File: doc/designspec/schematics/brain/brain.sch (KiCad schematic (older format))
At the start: 6 parts

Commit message: Add component lib
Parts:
- removed P?: Raspberry Pi 3 GPIO, symbol Raspberry~Pi~3~GPIO
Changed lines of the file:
@@
 $EndDescr
-$Comp
-L Raspberry~Pi~3~GPIO P?
-U 1 1 57FD3D22
-P 2800 2000
-F 0 "P?" H 2800 3050 50  0000 C CNN
-F 1 "Raspberry Pi 3 GPIO" V 2800 2000 50  0000 C CNN
-F 2 "" H 2800 1050 50  0000 C CNN
-F 3 "" H 2800 1050 50  0000 C CNN
-	1    2800 2000
-	1    0    0    -1
-$EndComp
 $Comp
 L USB_A P?
@@
 F 1 "CH340G" H 3800 4300 60  0000 C CNN
 F 2 "" H 3800 4300 60  0001 C CNN
-F 3 "" H 3800 4300 60  0001 C CNN
+F 3 "TODO: Choose component" H 3800 4300 60  0001 C CNN
 	1    3800 4300
 	-1   0    0    1
@@
 F 1 "CH340G" H 3800 3450 60  0000 C CNN
 F 2 "" H 3800 3450 60  0001 C CNN
-F 3 "" H 3800 3450 60  0001 C CNN
+F 3 "TODO: Choose component" H 3800 3450 60  0001 C CNN
 	1    3800 3450
 	-1   0    0    1

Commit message: Fix error for rpi_gpio in lib
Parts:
- added P?: Raspberry_pi_3_gpio, symbol Raspberry_pi_3_gpio
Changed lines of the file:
@@
 	1    0    0    -1
 $EndComp
-NoConn ~ 2350 2950
-NoConn ~ 2350 2850
-NoConn ~ 2350 2750
-NoConn ~ 2350 2650
-NoConn ~ 2350 2550
-NoConn ~ 2350 2450
-NoConn ~ 2350 2350
-NoConn ~ 2350 2250
-NoConn ~ 2350 2150
-NoConn ~ 2350 2050
-NoConn ~ 2350 1950
-NoConn ~ 2350 1850
-NoConn ~ 2350 1750
-NoConn ~ 2350 1650
-NoConn ~ 2350 1550
-NoConn ~ 2350 1450
-NoConn ~ 2350 1350
-NoConn ~ 2350 1250
-NoConn ~ 2350 1150
-NoConn ~ 2350 1050
+NoConn ~ 2750 2950
+NoConn ~ 2750 2850
+NoConn ~ 2750 2750
+NoConn ~ 2750 2650
+NoConn ~ 2750 2550
+NoConn ~ 2750 2450
+NoConn ~ 2750 2350
+NoConn ~ 2750 2250
+NoConn ~ 2750 2150
+NoConn ~ 2750 2050
+NoConn ~ 2750 1950
+NoConn ~ 2750 1850
+NoConn ~ 2750 1750
+NoConn ~ 2750 1650
+NoConn ~ 2750 1550
+NoConn ~ 2750 1450
+NoConn ~ 2750 1350
+NoConn ~ 2750 1250
+NoConn ~ 2750 1150
+NoConn ~ 2750 1050
 NoConn ~ 3250 1050
 NoConn ~ 3250 1150
@@
 NoConn ~ 3250 2650
 NoConn ~ 3250 2750
+$Comp
+L Raspberry_pi_3_gpio P?
+U 1 1 57FD5699
+P 3000 2000
+F 0 "P?" H 3000 3050 50  0000 C CNN
+F 1 "Raspberry_pi_3_gpio" V 3000 2000 50  0000 C CNN
+F 2 "" H 3000 1050 50  0000 C CNN
+F 3 "" H 3000 1050 50  0000 C CNN
+	1    3000 2000
+	1    0    0    -1
+$EndComp
 $EndSCHEMATC

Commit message: Fix rpi pins
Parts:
- removed P?: Raspberry_pi_3_gpio, symbol Raspberry_pi_3_gpio
- added P3: Raspberry Pi 3 GPIO, symbol Raspberry~Pi~3~GPIO
- gave numbers to parts that had none: 5
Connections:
- net labels added: +3.3V
- net labels removed: +5V
- wire segments 8 -> 10
- no-connect marks 42 -> 41
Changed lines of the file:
@@
 $EndDescr
 $Comp
-L USB_A P?
+L USB_A P2
 U 1 1 57FD3DF3
 P 2950 4250
-F 0 "P?" H 3150 4050 50  0000 C CNN
+F 0 "P2" H 3150 4050 50  0000 C CNN
 F 1 "USB_RPi_1" H 2900 4450 50  0000 C CNN
 F 2 "" V 2900 4150 50  0000 C CNN
@@
 $EndComp
 $Comp
-L USB_A P?
+L USB_A P1
 U 1 1 57FD409A
 P 2950 3400
-F 0 "P?" H 3150 3200 50  0000 C CNN
+F 0 "P1" H 3150 3200 50  0000 C CNN
 F 1 "USB_RPi_2" H 2900 3600 50  0000 C CNN
 F 2 "" V 2900 3300 50  0000 C CNN
@@
 $EndComp
 $Comp
-L CH340G U?
+L CH340G U2
 U 1 1 57FD4430
 P 3800 4300
-F 0 "U?" H 3450 4650 60  0000 C CNN
+F 0 "U2" H 3450 4650 60  0000 C CNN
 F 1 "CH340G" H 3800 4300 60  0000 C CNN
 F 2 "" H 3800 4300 60  0001 C CNN
@@
 $EndComp
 $Comp
-L CH340G U?
+L CH340G U1
 U 1 1 57FD4518
 P 3800 3450
-F 0 "U?" H 3450 3800 60  0000 C CNN
+F 0 "U1" H 3450 3800 60  0000 C CNN
 F 1 "CH340G" H 3800 3450 60  0000 C CNN
 F 2 "" H 3800 3450 60  0001 C CNN
@@
 $EndComp
 $Comp
-L BTN U?
+L BTN U3
 U 1 1 57FD4666
 P 3900 2800
-F 0 "U?" H 4050 2550 60  0000 C CNN
+F 0 "U3" H 4050 2550 60  0000 C CNN
 F 1 "BTN x2" H 3800 2800 60  0000 C CNN
 F 2 "" H 3900 2800 60  0001 C CNN
@@
 NoConn ~ 3500 2950
 $Comp
-L +5V #PWR?
-U 1 1 57FD4995
-P 4400 2650
-F 0 "#PWR?" H 4400 2500 50  0001 C CNN
-F 1 "+5V" H 4400 2790 50  0000 C CNN
-F 2 "" H 4400 2650 50  0000 C CNN
-F 3 "" H 4400 2650 50  0000 C CNN
-	1    4400 2650
-	1    0    0    -1
-$EndComp
-$Comp
-L GND #PWR?
+L GND #PWR01
 U 1 1 57FD49B5
 P 4400 2950
-F 0 "#PWR?" H 4400 2700 50  0001 C CNN
+F 0 "#PWR01" H 4400 2700 50  0001 C CNN
 F 1 "GND" H 4400 2800 50  0000 C CNN
 F 2 "" H 4400 2950 50  0000 C CNN
@@
 NoConn ~ 2750 1250
 NoConn ~ 2750 1150
-NoConn ~ 2750 1050
 NoConn ~ 3250 1050
 NoConn ~ 3250 1150
@@
 NoConn ~ 3250 2650
 NoConn ~ 3250 2750
+Wire Wire Line
+	2750 1050 2600 1050
 $Comp
-L Raspberry_pi_3_gpio P?
-U 1 1 57FD5699
+L +3.3V #PWR02
+U 1 1 57FE3030
+P 2600 1050
+F 0 "#PWR02" H 2600 900 50  0001 C CNN
+F 1 "+3.3V" H 2600 1190 50  0000 C CNN
+F 2 "" H 2600 1050 50  0000 C CNN
+F 3 "" H 2600 1050 50  0000 C CNN
+	1    2600 1050
+	1    0    0    -1
+$EndComp
+$Comp
+L +3.3V #PWR03
+U 1 1 57FE3059
+P 4400 2650
+F 0 "#PWR03" H 4400 2500 50  0001 C CNN
+F 1 "+3.3V" H 4400 2790 50  0000 C CNN
+F 2 "" H 4400 2650 50  0000 C CNN
+F 3 "" H 4400 2650 50  0000 C CNN
+	1    4400 2650
+	1    0    0    -1
+$EndComp
+$Comp
+L Raspberry~Pi~3~GPIO P3
+U 1 1 57FE33DC
 P 3000 2000
-F 0 "P?" H 3000 3050 50  0000 C CNN
-F 1 "Raspberry_pi_3_gpio" V 3000 2000 50  0000 C CNN
+F 0 "P3" H 3000 3050 50  0000 C CNN
+F 1 "Raspberry Pi 3 GPIO" V 3000 2000 50  0000 C CNN
 F 2 "" H 3000 1050 50  0000 C CNN
 F 3 "" H 3000 1050 50  0000 C CNN
@@
 	1    0    0    -1
 $EndComp
+Wire Wire Line
+	3250 1250 3450 1250
+$Comp
+L GND #PWR04
+U 1 1 57FE3423
+P 3450 1250
+F 0 "#PWR04" H 3450 1000 50  0001 C CNN
+F 1 "GND" H 3450 1100 50  0000 C CNN
+F 2 "" H 3450 1250 50  0000 C CNN
+F 3 "" H 3450 1250 50  0000 C CNN
+	1    3450 1250
+	1    0    0    -1
+$EndComp

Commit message: Fix RPI in lib (dont use spaces in component names)
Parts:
- removed P3: Raspberry Pi 3 GPIO, symbol Raspberry~Pi~3~GPIO
- added P3: RPi_3_GPIO, symbol RPi_3_GPIO
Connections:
- no-connect marks 41 -> 40
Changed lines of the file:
@@
 NoConn ~ 3250 1050
 NoConn ~ 3250 1150
-NoConn ~ 3250 1250
 NoConn ~ 3250 1350
 NoConn ~ 3250 1450
@@
 	1    0    0    -1
 $EndComp
-$Comp
-L Raspberry~Pi~3~GPIO P3
-U 1 1 57FE33DC
-P 3000 2000
-F 0 "P3" H 3000 3050 50  0000 C CNN
-F 1 "Raspberry Pi 3 GPIO" V 3000 2000 50  0000 C CNN
-F 2 "" H 3000 1050 50  0000 C CNN
-F 3 "" H 3000 1050 50  0000 C CNN
-	1    3000 2000
-	1    0    0    -1
-$EndComp
 Wire Wire Line
 	3250 1250 3450 1250
@@
 	1    0    0    -1
 $EndComp
+$Comp
+L RPi_3_GPIO P3
+U 1 1 57FE32EC
+P 3000 2000
+F 0 "P3" H 3000 3050 50  0000 C CNN
+F 1 "RPi_3_GPIO" V 3000 2000 50  0000 C CNN
+F 2 "" H 3000 1050 50  0000 C CNN
+F 3 "" H 3000 1050 50  0000 C CNN
+	1    3000 2000
+	1    0    0    -1
+$EndComp

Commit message: Use simple switch instead of button
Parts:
- removed U3: BTN x2, symbol BTN
- added SW? (x2): SPST, symbol SPST
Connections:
- no-connect marks 40 -> 38
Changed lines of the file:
@@
-	-1   0    0    1
-$EndComp
-$Comp
-L BTN U3
-U 1 1 57FD4666
-P 3900 2800
-F 0 "U3" H 4050 2550 60  0000 C CNN
-F 1 "BTN x2" H 3800 2800 60  0000 C CNN
-F 2 "" H 3900 2800 60  0001 C CNN
-F 3 "" H 3900 2800 60  0001 C CNN
-	1    3900 2800
 	-1   0    0    1
 $EndComp
 NoConn ~ 4400 4350
 NoConn ~ 4400 3500
-Wire Wire Line
-	4400 4550 4400 4450
-Wire Wire Line
-	4400 3700 4400 3600
-Wire Wire Line
-	3350 2650 3500 2650
-Wire Wire Line
-	3350 2650 3350 2850
-Wire Wire Line
-	3350 2850 3250 2850
-Wire Wire Line
-	3500 2850 3450 2850
-Wire Wire Line
-	3450 2850 3450 2950
-Wire Wire Line
-	3450 2950 3250 2950
-NoConn ~ 3500 2750
-NoConn ~ 3500 2950
-$Comp
-L GND #PWR01
-U 1 1 57FD49B5
-P 4400 2950
-F 0 "#PWR01" H 4400 2700 50  0001 C CNN
-F 1 "GND" H 4400 2800 50  0000 C CNN
-F 2 "" H 4400 2950 50  0000 C CNN
-F 3 "" H 4400 2950 50  0000 C CNN
-	1    4400 2950
-	1    0    0    -1
-$EndComp
 NoConn ~ 2750 2950
 NoConn ~ 2750 2850
@@
 NoConn ~ 3250 2650
 NoConn ~ 3250 2750
-Wire Wire Line
-	2750 1050 2600 1050
 $Comp
 L +3.3V #PWR02
@@
 L +3.3V #PWR03
 U 1 1 57FE3059
-P 4400 2650
-F 0 "#PWR03" H 4400 2500 50  0001 C CNN
-F 1 "+3.3V" H 4400 2790 50  0000 C CNN
-F 2 "" H 4400 2650 50  0000 C CNN
-F 3 "" H 4400 2650 50  0000 C CNN
-	1    4400 2650
+P 4550 2850
+F 0 "#PWR03" H 4550 2700 50  0001 C CNN
+F 1 "+3.3V" H 4550 2990 50  0000 C CNN
+F 2 "" H 4550 2850 50  0000 C CNN
+F 3 "" H 4550 2850 50  0000 C CNN
+	1    4550 2850
 	1    0    0    -1
 $EndComp
-Wire Wire Line
-	3250 1250 3450 1250
 $Comp
 L GND #PWR04
@@
 	1    0    0    -1
 $EndComp
+$Comp
+L SPST SW?
+U 1 1 580118F0
+P 3850 2700
+F 0 "SW?" H 3850 2800 50  0000 C CNN
+F 1 "SPST" H 3850 2600 50  0000 C CNN
+F 2 "" H 3850 2700 50  0000 C CNN
+F 3 "" H 3850 2700 50  0000 C CNN
+	1    3850 2700
+	1    0    0    -1
+$EndComp
+Wire Wire Line
+	4400 4550 4400 4450
+Wire Wire Line
+	4400 3700 4400 3600
+Wire Wire Line
+	3350 2850 3250 2850
+Wire Wire Line
+	2750 1050 2600 1050
+Wire Wire Line
+	3250 1250 3450 1250
+Wire Wire Line
+	3350 2700 3350 2850
+$Comp
+L SPST SW?
+U 1 1 58011A78
+P 3850 3000
+F 0 "SW?" H 3850 3100 50  0000 C CNN
+F 1 "SPST" H 3850 2900 50  0000 C CNN
+F 2 "" H 3850 3000 50  0000 C CNN
+F 3 "" H 3850 3000 50  0000 C CNN
+	1    3850 3000
+	1    0    0    -1
+$EndComp
+Wire Wire Line
+	4350 2700 4350 3000
+Wire Wire Line
+	3250 2950 3350 2950
+Wire Wire Line
+	3350 2950 3350 3000
+Wire Wire Line
+	4350 2850 4550 2850
+Connection ~ 4350 2850
 $EndSCHEMATC

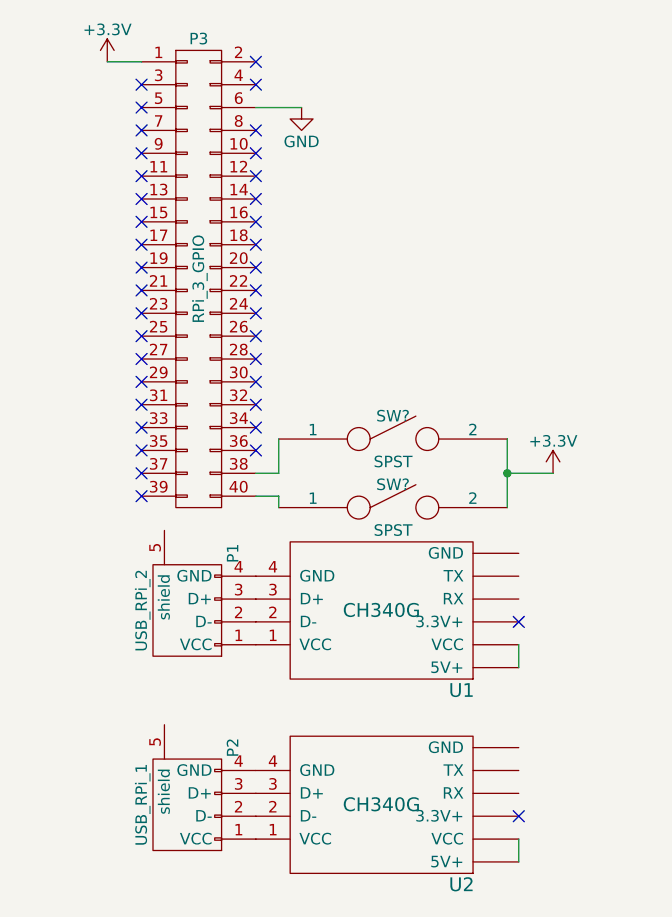
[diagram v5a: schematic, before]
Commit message: Replace CH340G with general USB-UART
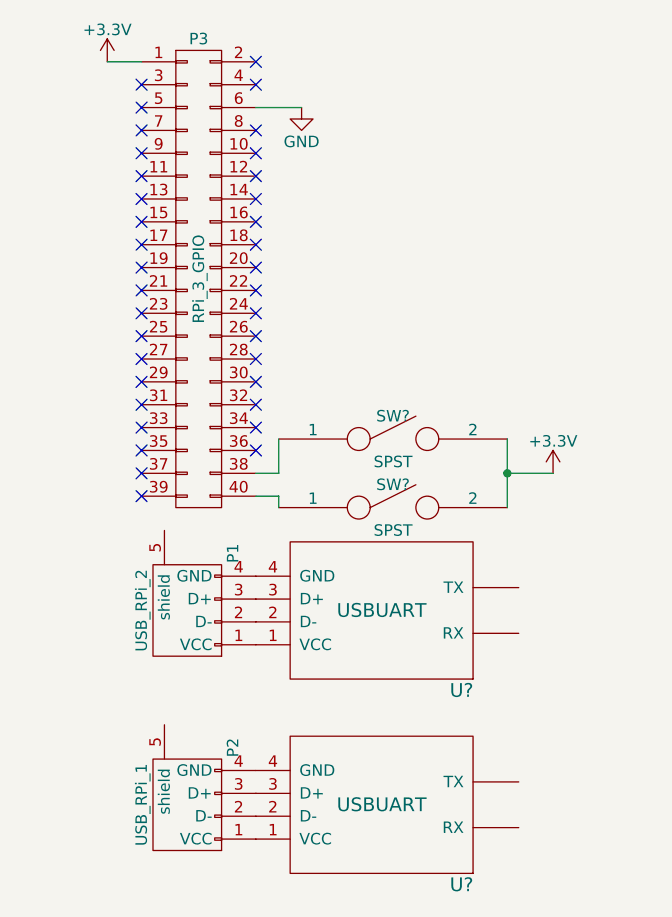
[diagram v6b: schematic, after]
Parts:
- removed U1, U2: CH340G, symbol CH340G
- added U? (x2): USBUART, symbol USBUART
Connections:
- net at P2.1 (VCC): now also U?.1 (VCC)
- net at P2.2 (D-): now also U?.2 (D-)
- net at P2.3 (D+): now also U?.3 (D+)
- net at P2.4 (GND): now also U?.4 (GND)
- net at P1.1 (VCC): now also U?.1 (VCC)
- net at P1.2 (D-): now also U?.2 (D-)
- net at P1.3 (D+): now also U?.3 (D+)
- net at P1.4 (GND): now also U?.4 (GND)
- no-connect marks 38 -> 36
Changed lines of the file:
@@
 	0    -1   -1   0
 $EndComp
-$Comp
-L CH340G U2
-U 1 1 57FD4430
-P 3800 4300
-F 0 "U2" H 3450 4650 60  0000 C CNN
-F 1 "CH340G" H 3800 4300 60  0000 C CNN
-F 2 "" H 3800 4300 60  0001 C CNN
-F 3 "TODO: Choose component" H 3800 4300 60  0001 C CNN
-	1    3800 4300
-	-1   0    0    1
-$EndComp
-$Comp
-L CH340G U1
-U 1 1 57FD4518
-P 3800 3450
-F 0 "U1" H 3450 3800 60  0000 C CNN
-F 1 "CH340G" H 3800 3450 60  0000 C CNN
-F 2 "" H 3800 3450 60  0001 C CNN
-F 3 "TODO: Choose component" H 3800 3450 60  0001 C CNN
-	1    3800 3450
-	-1   0    0    1
-$EndComp
-NoConn ~ 4400 4350
-NoConn ~ 4400 3500
 NoConn ~ 2750 2950
 NoConn ~ 2750 2850
@@
 $EndComp
 Wire Wire Line
-	4400 4550 4400 4450
-Wire Wire Line
-	4400 3700 4400 3600
-Wire Wire Line
 	3350 2850 3250 2850
 Wire Wire Line
@@
 $EndComp
 Wire Wire Line
-	4350 2700 4350 3000
+	4350 2700 4350 2850
+Wire Wire Line
+	4350 2850 4350 3000
 Wire Wire Line
 	3250 2950 3350 2950
@@
 	4350 2850 4550 2850
 Connection ~ 4350 2850
+$Comp
+L USBUART U?
+U 1 1 58013042
+P 3800 3450
+F 0 "U?" H 3450 3800 60  0000 C CNN
+F 1 "USBUART" H 3800 3450 60  0000 C CNN
+F 2 "" H 3800 3450 60  0001 C CNN
+F 3 "" H 3800 3450 60  0001 C CNN
+	1    3800 3450
+	-1   0    0    1
+$EndComp
+$Comp
+L USBUART U?
+U 1 1 58013123
+P 3800 4300
+F 0 "U?" H 3450 4650 60  0000 C CNN
+F 1 "USBUART" H 3800 4300 60  0000 C CNN
+F 2 "" H 3800 4300 60  0001 C CNN
+F 3 "" H 3800 4300 60  0001 C CNN
+	1    3800 4300
+	-1   0    0    1
+$EndComp
 $EndSCHEMATC

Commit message: Add button to brain schematics
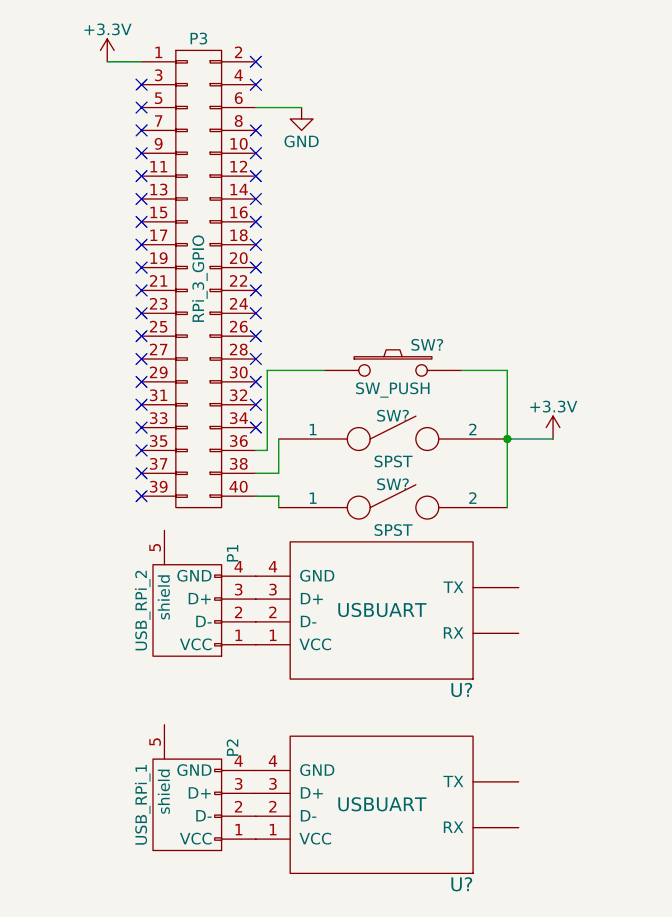
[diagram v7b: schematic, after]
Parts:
- added SW?: SW_PUSH, symbol SW_PUSH
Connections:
- net +3V3: now also SW?.2
- net at P3.36 (P36): now also SW?.1
- no-connect marks 36 -> 35
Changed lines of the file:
@@
 NoConn ~ 3250 2550
 NoConn ~ 3250 2650
-NoConn ~ 3250 2750
 $Comp
 L +3.3V #PWR02
@@
 L +3.3V #PWR03
 U 1 1 57FE3059
-P 4550 2850
-F 0 "#PWR03" H 4550 2700 50  0001 C CNN
-F 1 "+3.3V" H 4550 2990 50  0000 C CNN
-F 2 "" H 4550 2850 50  0000 C CNN
-F 3 "" H 4550 2850 50  0000 C CNN
-	1    4550 2850
+P 4550 2700
+F 0 "#PWR03" H 4550 2550 50  0001 C CNN
+F 1 "+3.3V" H 4550 2840 50  0000 C CNN
+F 2 "" H 4550 2700 50  0000 C CNN
+F 3 "" H 4550 2700 50  0000 C CNN
+	1    4550 2700
 	1    0    0    -1
 $EndComp
@@
 $EndComp
 Wire Wire Line
-	4350 2700 4350 2850
-Wire Wire Line
-	4350 2850 4350 3000
+	4350 2400 4350 3000
 Wire Wire Line
 	3250 2950 3350 2950
 Wire Wire Line
 	3350 2950 3350 3000
-Wire Wire Line
-	4350 2850 4550 2850
-Connection ~ 4350 2850
 $Comp
 L USBUART U?
@@
 	-1   0    0    1
 $EndComp
+$Comp
+L SW_PUSH SW?
+U 1 1 5804F9B6
+P 3850 2400
+F 0 "SW?" H 4000 2510 50  0000 C CNN
+F 1 "SW_PUSH" H 3850 2320 50  0000 C CNN
+F 2 "" H 3850 2400 50  0000 C CNN
+F 3 "" H 3850 2400 50  0000 C CNN
+	1    3850 2400
+	1    0    0    -1
+$EndComp
+Wire Wire Line
+	3550 2400 3300 2400
+Wire Wire Line
+	3300 2400 3300 2750
+Wire Wire Line
+	3300 2750 3250 2750
+Wire Wire Line
+	4150 2400 4350 2400
+Connection ~ 4350 2700
+Wire Wire Line
+	4550 2700 4350 2700
 $EndSCHEMATC

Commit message: Use two buttons with brain. Switch does not belong here.
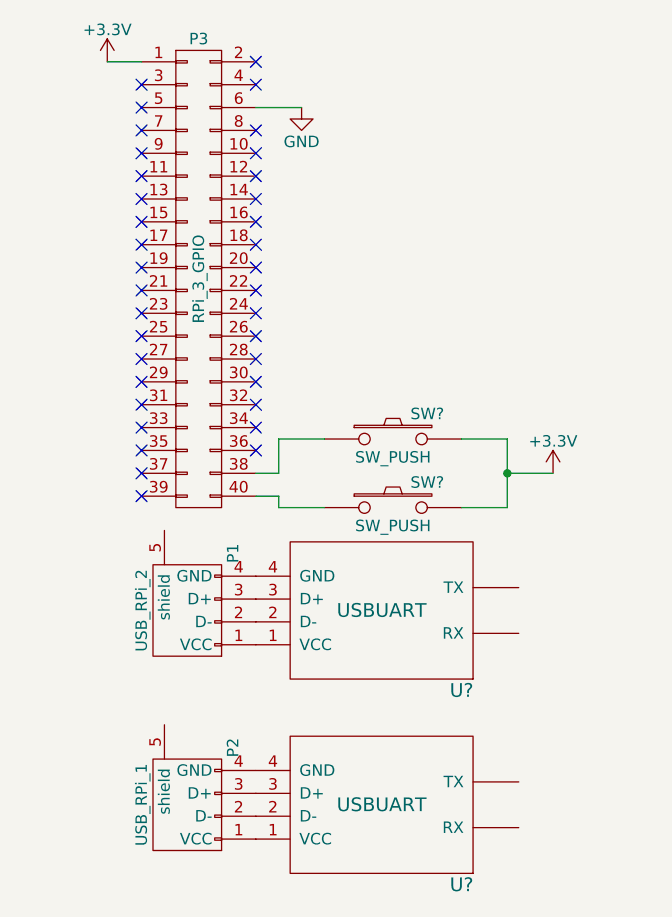
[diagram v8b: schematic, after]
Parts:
- removed SW? (x2): SPST, symbol SPST
- added SW?: SW_PUSH, symbol SW_PUSH
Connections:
- net +3V3: now also SW?.2
- net at P3.36 (P36): no longer SW?.1
- net at P3.38 (P38): now also SW?.1
- net at P3.40 (P40): now also SW?.1
- no-connect marks 35 -> 36
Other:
- moved on the sheet: SW?
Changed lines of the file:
@@
 L +3.3V #PWR03
 U 1 1 57FE3059
-P 4550 2700
-F 0 "#PWR03" H 4550 2550 50  0001 C CNN
-F 1 "+3.3V" H 4550 2840 50  0000 C CNN
-F 2 "" H 4550 2700 50  0000 C CNN
-F 3 "" H 4550 2700 50  0000 C CNN
-	1    4550 2700
+P 4550 2850
+F 0 "#PWR03" H 4550 2700 50  0001 C CNN
+F 1 "+3.3V" H 4550 2990 50  0000 C CNN
+F 2 "" H 4550 2850 50  0000 C CNN
+F 3 "" H 4550 2850 50  0000 C CNN
+	1    4550 2850
 	1    0    0    -1
 $EndComp
@@
 	1    0    0    -1
 $EndComp
-$Comp
-L SPST SW?
-U 1 1 580118F0
-P 3850 2700
-F 0 "SW?" H 3850 2800 50  0000 C CNN
-F 1 "SPST" H 3850 2600 50  0000 C CNN
-F 2 "" H 3850 2700 50  0000 C CNN
-F 3 "" H 3850 2700 50  0000 C CNN
-	1    3850 2700
-	1    0    0    -1
-$EndComp
 Wire Wire Line
 	3350 2850 3250 2850
@@
 Wire Wire Line
 	3350 2700 3350 2850
-$Comp
-L SPST SW?
-U 1 1 58011A78
-P 3850 3000
-F 0 "SW?" H 3850 3100 50  0000 C CNN
-F 1 "SPST" H 3850 2900 50  0000 C CNN
-F 2 "" H 3850 3000 50  0000 C CNN
-F 3 "" H 3850 3000 50  0000 C CNN
-	1    3850 3000
-	1    0    0    -1
-$EndComp
-Wire Wire Line
-	4350 2400 4350 3000
 Wire Wire Line
 	3250 2950 3350 2950
@@
 L SW_PUSH SW?
 U 1 1 5804F9B6
-P 3850 2400
-F 0 "SW?" H 4000 2510 50  0000 C CNN
-F 1 "SW_PUSH" H 3850 2320 50  0000 C CNN
-F 2 "" H 3850 2400 50  0000 C CNN
-F 3 "" H 3850 2400 50  0000 C CNN
-	1    3850 2400
+P 3850 2700
+F 0 "SW?" H 4000 2810 50  0000 C CNN
+F 1 "SW_PUSH" H 3850 2620 50  0000 C CNN
+F 2 "" H 3850 2700 50  0000 C CNN
+F 3 "" H 3850 2700 50  0000 C CNN
+	1    3850 2700
 	1    0    0    -1
 $EndComp
 Wire Wire Line
-	3550 2400 3300 2400
+	3550 2700 3350 2700
+NoConn ~ 3250 2750
 Wire Wire Line
-	3300 2400 3300 2750
+	4550 2850 4350 2850
+Connection ~ 4350 2850
 Wire Wire Line
-	3300 2750 3250 2750
+	4150 2700 4350 2700
 Wire Wire Line
-	4150 2400 4350 2400
-Connection ~ 4350 2700
+	4350 2700 4350 3000
+$Comp
+L SW_PUSH SW?
+U 1 1 5804FFC9
+P 3850 3000
+F 0 "SW?" H 4000 3110 50  0000 C CNN
+F 1 "SW_PUSH" H 3850 2920 50  0000 C CNN
+F 2 "" H 3850 3000 50  0000 C CNN
+F 3 "" H 3850 3000 50  0000 C CNN
+	1    3850 3000
+	1    0    0    -1
+$EndComp
 Wire Wire Line
-	4550 2700 4350 2700
+	4350 3000 4150 3000
+Wire Wire Line
+	3350 3000 3550 3000
 $EndSCHEMATC
